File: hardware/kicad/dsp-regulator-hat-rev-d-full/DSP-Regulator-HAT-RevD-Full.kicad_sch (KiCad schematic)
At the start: 0 parts

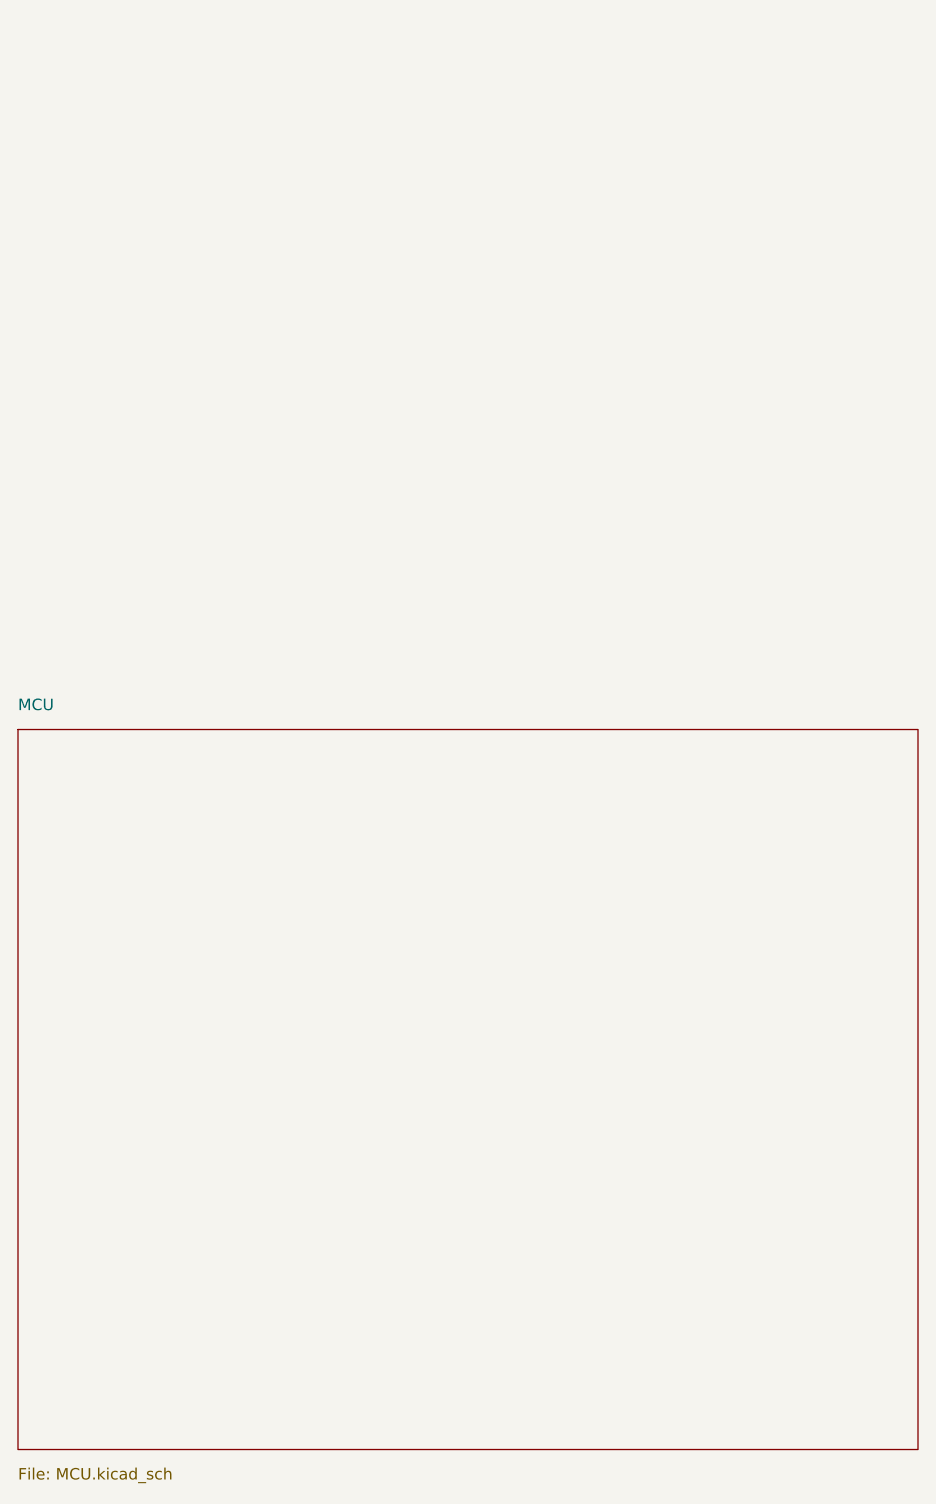
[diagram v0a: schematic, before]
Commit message: hw(hat): start source-backed Rev-D HAT integration
Import an independent HAT reuse sheet, replace legacy controller endpoints with frozen F405 interfaces and reset biases, and record partial-integration gaps and unresolved inherited ERC warnings. Support-only and Rev-C sources remain byte-identical; no PCB or bench validation claimed.

Co-authored-by: Copilot App <223556219+Copilot@users.noreply.github.com>
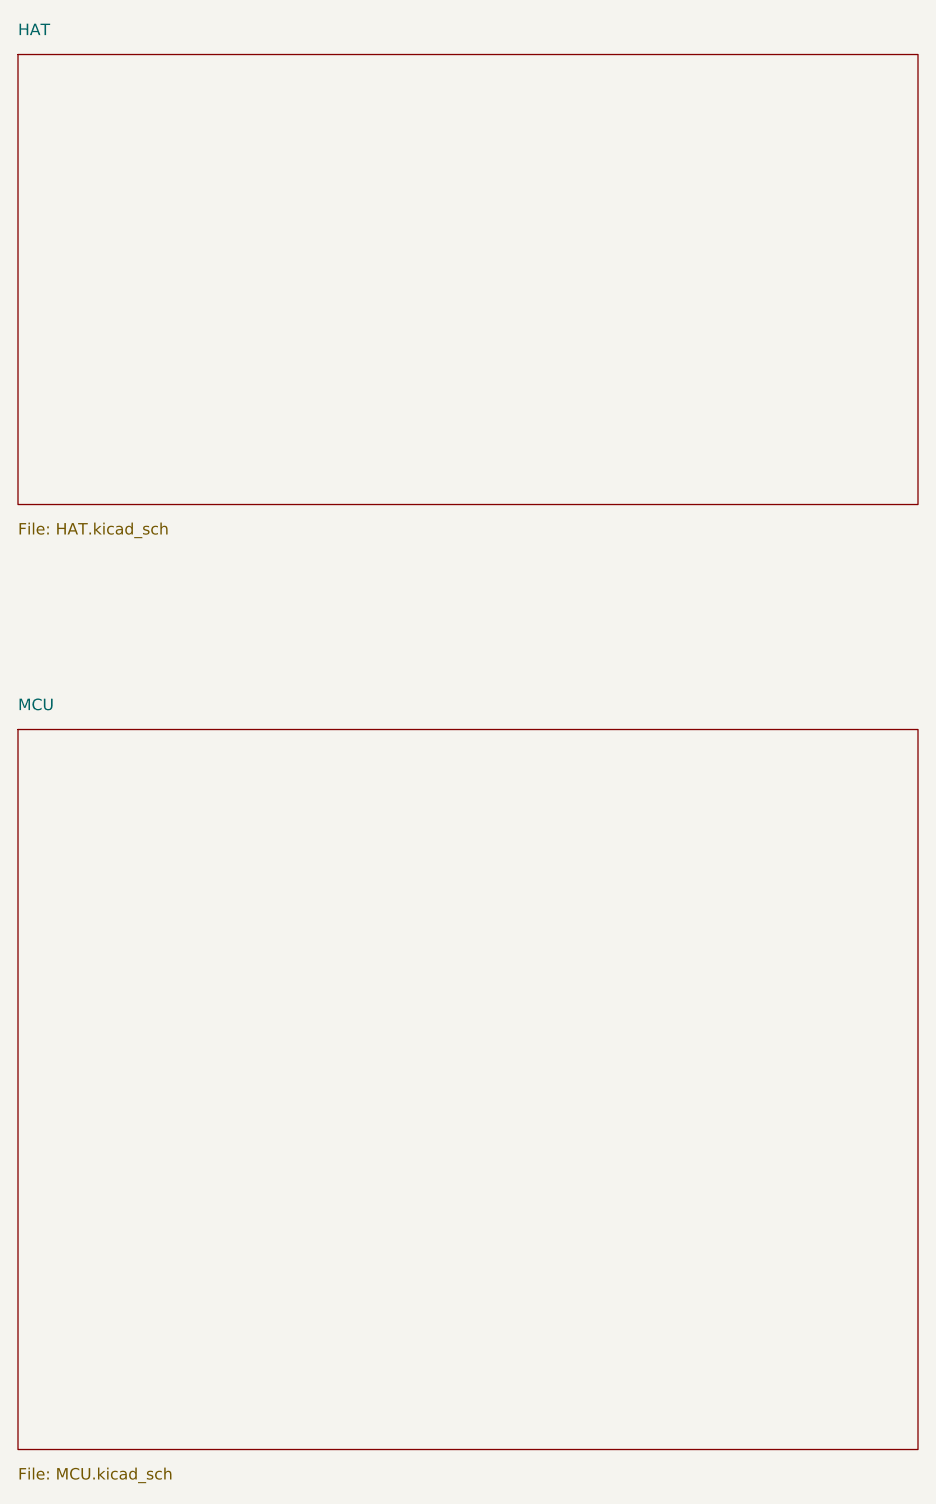
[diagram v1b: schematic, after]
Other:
- added sheet HAT (HAT.kicad_sch)
- title: DSP Regulator HAT Rev-D Full - Integration Starter -> DSP Regulator HAT Rev-D Full - Initial Integration
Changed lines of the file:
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@@
   (paper "A4")
   (title_block
-    (title "DSP Regulator HAT Rev-D Full - Integration Starter")
-    (rev "D / integration starter")
-    (comment 1 "Support circuits only; full HAT integration pending; not fabrication ready")
+    (title "DSP Regulator HAT Rev-D Full - Initial Integration")
+    (rev "D / first pass")
+    (comment 1 "Partial HAT reuse integration; bare C3 and missing source blocks pending; NOT RELEASED")
   )
   (sheet
+    (at 100 25)
+    (size 100 50)
+    (fields_autoplaced yes)
+    (stroke (width 0) (type default))
+    (fill (color 0 0 0 0))
+    (property "Sheet name" "HAT" (at 100 23 0)
+      (effects (font (size 1.27 1.27)) (justify left bottom)))
+    (property "Sheet file" "HAT.kicad_sch" (at 100 77 0)
+      (effects (font (size 1.27 1.27)) (justify left top)))
+    (instances
+      (project "DSP-Regulator-HAT-RevD-Full"
+        (path "/8eac47b6-9c92-4005-8483-c8ba2676659b" (page "3"))
+      )
+    )
+  )
+  (sheet
